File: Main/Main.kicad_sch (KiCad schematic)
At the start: 34 parts, among them IC1 L9110S, IC2 L9110S, IC3 L9110S, J1 Conn_01x10_Female, J2 I2C_STANDARDQWIIC, J3 Conn_01x02_Female, J4 Conn_01x05_Female, J5 Conn_01x05_Female, J6 Conn_01x05_Female, J7 Conn_01x12_Female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

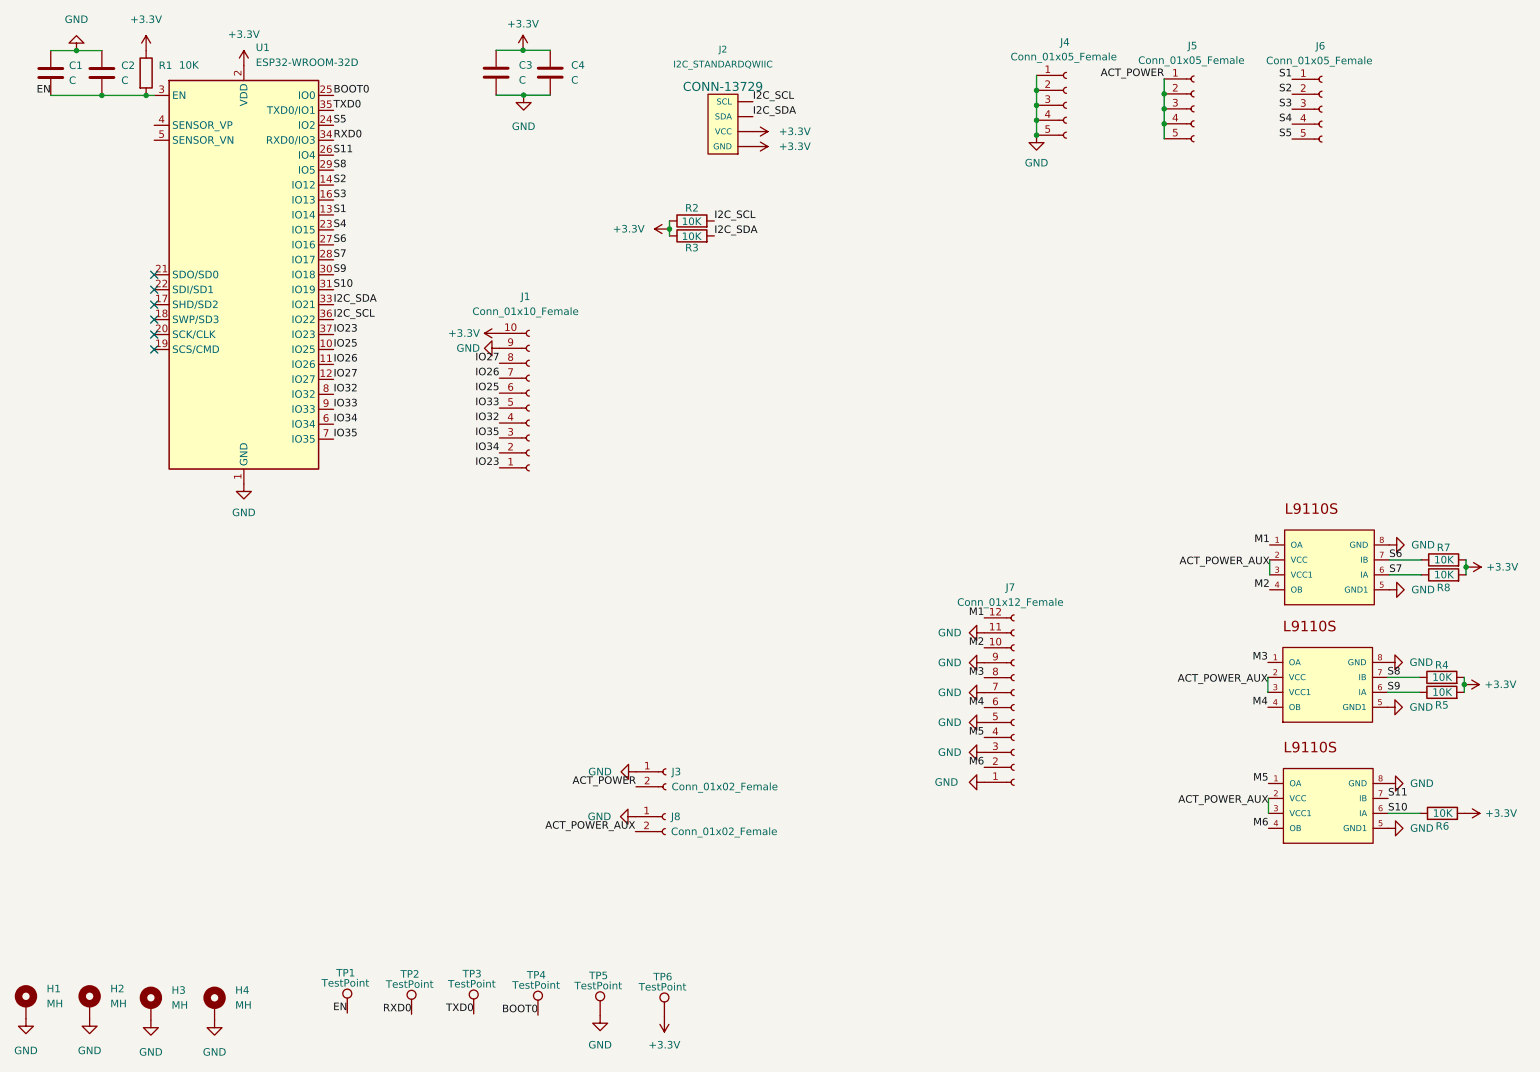
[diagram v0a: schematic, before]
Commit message: main board : improve silkscreen, LCSC sourcing, capacitor value and JLCPCB files
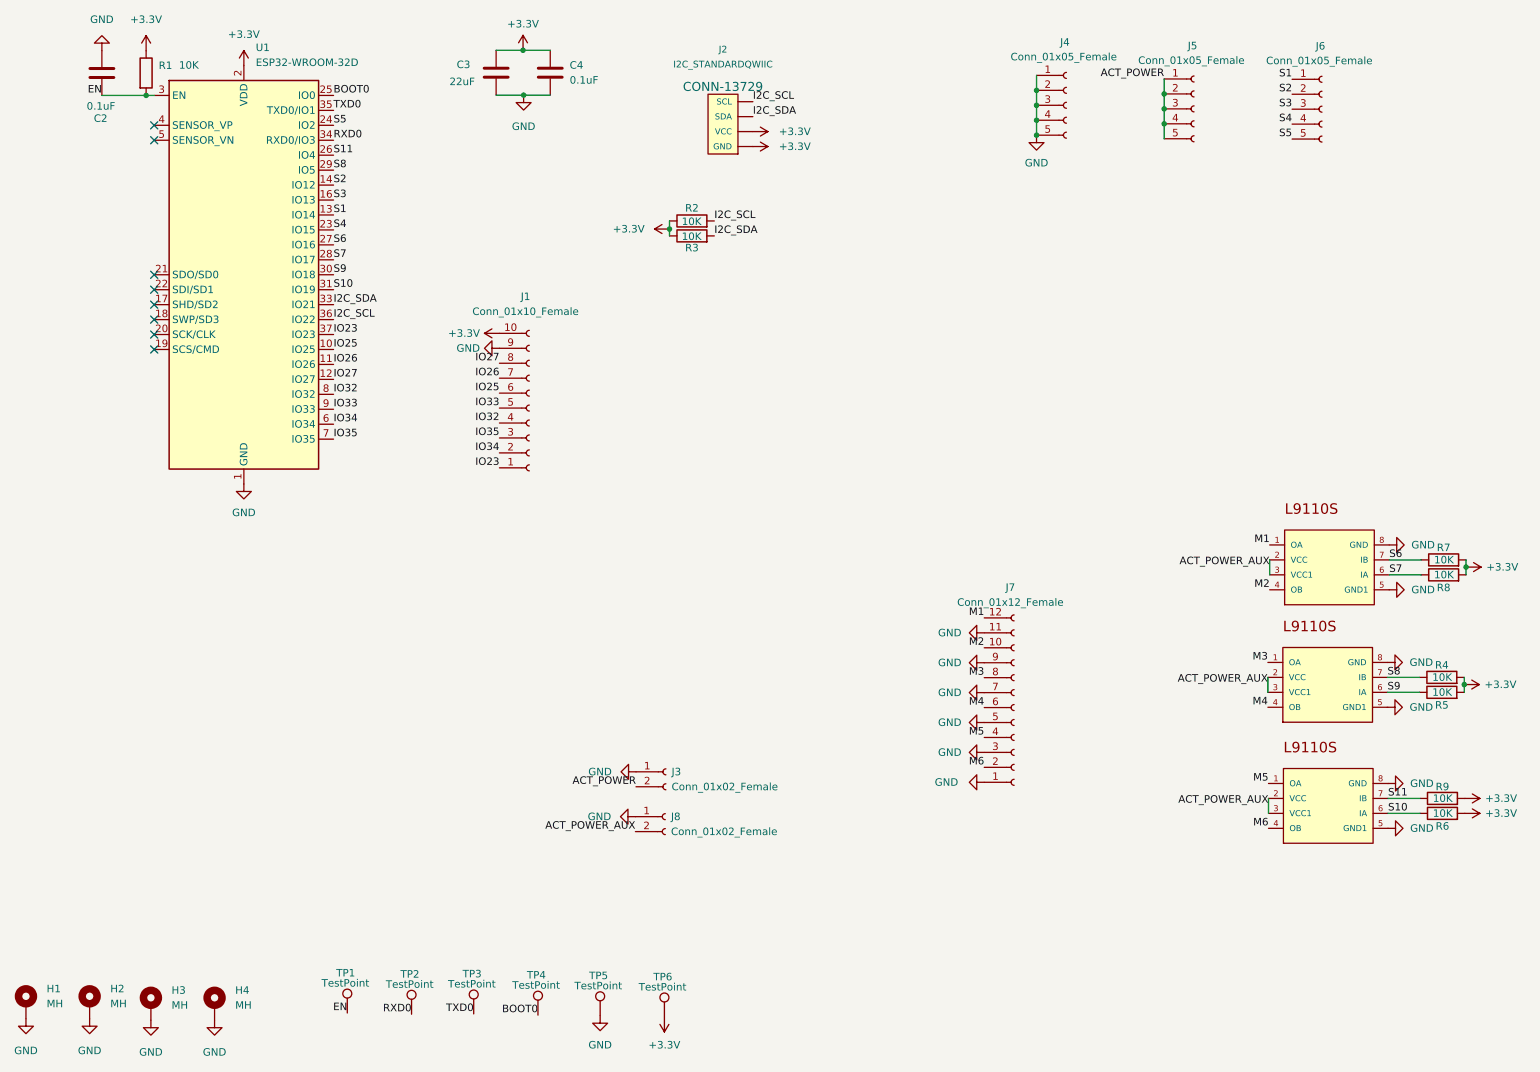
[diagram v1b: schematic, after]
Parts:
- removed C1: C, Capacitor_SMD:C_0402_1005Metric, symbol Device:C
- added R9: 10K, Resistor_SMD:R_0402_1005Metric, symbol Device:R
- C2, C4: value C -> 0.1uF; LCSC (none) -> C178771
- C3: value C -> 22uF; LCSC (none) -> C2836678
- IC1, IC2, IC3: LCSC (none) -> C2984833
- R1, R2, R3, R4, R5, R6, R7, R8: LCSC (none) -> C325396
- U1: LCSC (none) -> C473012
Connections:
- net +3V3: now also R9.2
- net S11: now also R9.1
- no-connect marks 6 -> 8
